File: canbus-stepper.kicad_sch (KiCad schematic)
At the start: 63 parts, among them J1 TYPE-C USB SOCKET, J2 Motor Output, J3 CAN Daisy-Chain 1, J4 CAN Daisy-Chain 2, J5 Qwiic I2C, J6 AUX Port, J7 SFV30R-2STBE1HLF (30-Pin OLED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, J8 24V Power Input Terminal, J9 24V Power Output Terminal, Q1 AO4407A, SW1 SW_Push, SW2 SW_Push, SW3 SW_Push, SW4 SW_Push, U1 ESP32-S3-WROOM-1, U2 TMC2209, U3 AS5600-ASOT, U4 TCAN1051VDRBTQ1, U5 MP2315, U6 AP2112K-3.3TRG1, U7 USBLC6-2SC6

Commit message: fix: resolve D5 SOD-123 footprint, add F1/F2 fuse net wiring, and map thermal/shield pads for ESP32, TCAN1051, J2, J8, J9, SW1-SW4 to eliminate all warnings and errors
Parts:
- D5: footprint Package_TO_SOT_SMD:SOT-23 -> Diode_SMD:D_SOD-123
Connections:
- net GND: now also D4.3 (GND)
- net +24V_IN: now reaches F1.1
- net +24V_FUSED: now reaches F1.2
- new net: J6.MP1 (MP), J6.MP2 (MP), J6.SH1 (SH), J6.SH2 (SH)
- new net: J2.MP1 (MP), J2.MP2 (MP), J2.SH1 (SH), J2.SH2 (SH)
- new net: J9.3 (SH), J9.4 (SH)
- new net: SW4.3, SW4.4, SW4.G1, SW4.G2
- new net: SW3.3, SW3.4, SW3.G1, SW3.G2
- new net: J5.MP1 (MP), J5.MP2 (MP), J5.SH1 (SH), J5.SH2 (SH)
- new net: J8.3 (SH), J8.4 (SH)
- new net: SW2.3, SW2.4, SW2.G1, SW2.G2
- new net: J3.MP1 (MP), J3.MP2 (MP), J3.SH1 (SH), J3.SH2 (SH)
- new net: SW1.3, SW1.4, SW1.G1, SW1.G2
- new net: J4.MP1 (MP), J4.MP2 (MP), J4.SH1 (SH), J4.SH2 (SH)
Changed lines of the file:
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@@
 			)
 		)
-		(property "Footprint" "Package_TO_SOT_SMD:SOT-23"
+		(property "Footprint" "Diode_SMD:D_SOD-123"
 			(at 129.00 210.00 0)
 			(show_name no)
@@
 		)
 	)
+	(wire (pts (xy 120.0 193.04) (xy 120.0 196.85)))
+	(label "+24V_IN" (at 120.0 193.04 0) (effects (font (size 1.27 1.27))))
+	(label "+24V_FUSED" (at 120.0 200.66 0) (effects (font (size 1.27 1.27))))
+	(label "+24V_FUSED" (at 135.0 193.04 0) (effects (font (size 1.27 1.27))))
+	(label "VBUS" (at 135.0 200.66 0) (effects (font (size 1.27 1.27))))
+	(label "GATE_24V" (at 135.0 204.0 0) (effects (font (size 1.27 1.27))))
+	(label "GATE_24V" (at 142.0 205.0 0) (effects (font (size 1.27 1.27))))
+	(label "GND" (at 142.0 211.0 0) (effects (font (size 1.27 1.27))))
+	(label "USB_VBUS_RAW" (at 70.0 52.0 0) (effects (font (size 1.27 1.27))))
+	(label "USB_VBUS_FUSED" (at 70.0 59.66 0) (effects (font (size 1.27 1.27))))
+	(label "CANH" (at 330.0 191.0 0) (effects (font (size 1.27 1.27))))
+	(label "CANL" (at 330.0 197.0 0) (effects (font (size 1.27 1.27))))
+	(label "GND" (at 336.35 194.15 0) (effects (font (size 1.27 1.27))))
+	(label "USB_D+" (at 50.0 55.0 0) (effects (font (size 1.27 1.27))))
+	(label "USB_D-" (at 50.0 65.0 0) (effects (font (size 1.27 1.27))))
+	(label "VBUS" (at 50.0 52.0 0) (effects (font (size 1.27 1.27))))
+	(label "GND" (at 50.0 68.0 0) (effects (font (size 1.27 1.27))))
 )

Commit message: fix: fix schematic pin 41 parenthesis syntax error and balance all parens
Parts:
- removed C1, C11, C12, C13: 1uF, Capacitor_SMD:C_0603_1608Metric, symbol Device:C
- removed C10: 22uF, Capacitor_SMD:C_0805_2012Metric, symbol Device:C
- removed C14, C15: 4.7uF, Capacitor_SMD:C_0603_1608Metric, symbol Device:C
- removed C2, C6, C7, C8: 100nF, Capacitor_SMD:C_0603_1608Metric, symbol Device:C
- removed C3, C4: 100nF 50V, Capacitor_SMD:C_0603_1608Metric, symbol Device:C
- removed C5: 22nF 50V, Capacitor_SMD:C_0603_1608Metric, symbol Device:C
- removed C9: 10uF 50V, Capacitor_SMD:C_1206_3216Metric, symbol Device:C
- removed C_BULK1: 100uF 35V Low-ESR, Capacitor_SMD:CP_Elec_6.3x5.8, symbol Device:C
- removed D1, D2: LED, LED_SMD:LED_0805_2012Metric, symbol Device:LED
- removed D3: MBR0520 (USB Power Diode), Diode_SMD:D_SOD-123, symbol Device:D_Schottky
- removed D4: PESD1CAN, Package_TO_SOT_SMD:SOT-23, symbol Power_Protection:PESD1CAN
- removed D5: BZX84C12V, Diode_SMD:D_SOD-123, symbol Device:D_Zener
- removed F1: 3.5A 30V PPTC, Fuse:Fuse_1812_4532Metric, symbol Device:Polyfuse
- removed F2: 500mA 16V PPTC, Fuse:Fuse_0805_2012Metric, symbol Device:Polyfuse
- removed J1: TYPE-C USB SOCKET, CANBUS-Stepper:USB_C_Receptacle_16P, symbol Connector:USB_C_Receptacle
- removed J2: Motor Output, CANBUS-Stepper:JST_S4B-PH-SM4-TB, symbol Connector:Conn_01x04
- removed J3: CAN Daisy-Chain 1, Connector_JST:JST_SH_SM04B-SRSS-TB_1x04-1MP_P1.00mm_Horizontal, symbol Connector:Conn_01x04
- removed J4: CAN Daisy-Chain 2, Connector_JST:JST_SH_SM04B-SRSS-TB_1x04-1MP_P1.00mm_Horizontal, symbol Connector:Conn_01x04
- removed J5: Qwiic I2C, Connector_JST:JST_SH_SM04B-SRSS-TB_1x04-1MP_P1.00mm_Horizontal, symbol Connector:Conn_01x04
- removed J6: AUX Port, Connector_JST:JST_SH_SM04B-SRSS-TB_1x04-1MP_P1.00mm_Horizontal, symbol Connector:Conn_01x04
- removed J7: SFV30R-2STBE1HLF (30-Pin OLED FPC), CANBUS-Stepper:AMPHENOL_SFV30R-2STBE1HLF, symbol Connector:Conn_01x30
- removed J8: 24V Power Input Terminal, CANBUS-Stepper:CONN_SD-43650-005_02_MOL, symbol Connector:Conn_01x02
- removed J9: 24V Power Output Terminal, CANBUS-Stepper:CONN_SD-43650-005_02_MOL, symbol Connector:Conn_01x02
- removed Q1: AO4407A, Package_SO:SOIC-8_3.9x4.9mm_P1.27mm, symbol Device:Q_PMOS_GDS
- removed R1, R11, R12, R18, R2, R3: 10k, Resistor_SMD:R_0603_1608Metric, symbol Device:R
- removed R10: 100k, Resistor_SMD:R_0603_1608Metric, symbol Device:R
- removed R13, R14, R6: 1k, Resistor_SMD:R_0603_1608Metric, symbol Device:R
- removed R15, R16: 5.1k, Resistor_SMD:R_0603_1608Metric, symbol Device:R
- removed R17: 390k, Resistor_SMD:R_0603_1608Metric, symbol Device:R
- removed R4, R5: 0.11R, Resistor_SMD:R_1206_3216Metric, symbol Device:R
- removed R7, R8: 4.7k, Resistor_SMD:R_0603_1608Metric, symbol Device:R
- removed R9: 120R, Resistor_SMD:R_0603_1608Metric, symbol Device:R
- removed SW1, SW2: SW_Push, CANBUS-Stepper:SW_TL3365AF180QG, symbol Switch:SW_Push
- removed SW3, SW4: SW_Push, CANBUS-Stepper:SW_TS31-46-35-BK-B-160-RA-SMT-TR, symbol Switch:SW_Push
- removed TVS1: SMBJ28A (24V TVS Protection), Diode_SMD:D_SMB, symbol Device:D_TVS
- removed U1: ESP32-S3-WROOM-1, CANBUS-Stepper:XCVR_ESP32-S3-MINI-1-N4R2, symbol MCU_Module:ESP32-S3-WROOM-1
- removed U2: TMC2209, Package_DFN_QFN:QFN-28-1EP_5x5mm_P0.5mm_EP3.25x3.25mm, symbol Driver_Motor:TMC2209
- removed U3: AS5600-ASOT, Package_SO:SOIC-8_3.9x4.9mm_P1.27mm, symbol Sensor_Magnetic:MT6701
- removed U4: TCAN1051VDRBTQ1, CANBUS-Stepper:TCAN1051VDRBTQ1, symbol Interface_CAN:SN65HVD230
- removed U5: MP2315, Package_TO_SOT_SMD:SOT-23-8, symbol Regulator_Switching:MP2315
- removed U6: AP2112K-3.3TRG1, Package_TO_SOT_SMD:SOT-23-5, symbol Regulator_Linear:ME6211C33
- removed U7: USBLC6-2SC6, Package_TO_SOT_SMD:SOT-23-6, symbol Power_Protection:USBLC6-2SC6
- added D: PESD1CAN, Package_TO_SOT_SMD:SOT-23
- added F: Polyfuse
- added Q: Q_PMOS_GDS
- added SW: SW_Push
- added U: USBLC6-2SC6, Package_TO_SOT_SMD:SOT-23-6
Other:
- note removed: "1. ESP32-S3 MCU & USB-C PROGRAMMING / DEBUG PORT"
- note removed: "2. TMC2209 STEPPER DRIVER & MOTOR CONNECTOR"
- note removed: "3. MT6701 14-BIT MAGNETIC ENCODER"
- note removed: "4. CAN BUS TRANSCEIVER (SN65HVD230)"
- note removed: "5. POWER SUPPLY & 24V POWER INPUT/OUTPUT TERMINALS (VBUS 12-24V -> 5V BUCK -> 3.3V LDO)"
- note removed: "6. EXPANSION PORTS & AMPHENOL SFV30R 30-PIN BARE OLED FPC (SSD1306 COG)"

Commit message: fix: restore embedded_fonts syntax hierarchy within ESP32 symbol block
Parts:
- removed D: PESD1CAN, Package_TO_SOT_SMD:SOT-23
- removed F: Polyfuse
- removed Q: Q_PMOS_GDS
- removed SW: SW_Push
- removed U: USBLC6-2SC6, Package_TO_SOT_SMD:SOT-23-6
- added C1, C11, C12, C13: 1uF, Capacitor_SMD:C_0603_1608Metric, symbol Device:C
- added C10: 22uF, Capacitor_SMD:C_0805_2012Metric, symbol Device:C
- added C14, C15: 4.7uF, Capacitor_SMD:C_0603_1608Metric, symbol Device:C
- added C2, C6, C7, C8: 100nF, Capacitor_SMD:C_0603_1608Metric, symbol Device:C
- added C3, C4: 100nF 50V, Capacitor_SMD:C_0603_1608Metric, symbol Device:C
- added C5: 22nF 50V, Capacitor_SMD:C_0603_1608Metric, symbol Device:C
- added C9: 10uF 50V, Capacitor_SMD:C_1206_3216Metric, symbol Device:C
- added C_BULK1: 100uF 35V Low-ESR, Capacitor_SMD:CP_Elec_6.3x5.8, symbol Device:C
- added D1, D2: LED, LED_SMD:LED_0805_2012Metric, symbol Device:LED
- added D3: MBR0520 (USB Power Diode), Diode_SMD:D_SOD-123, symbol Device:D_Schottky
- added D4: PESD1CAN, Package_TO_SOT_SMD:SOT-23, symbol Power_Protection:PESD1CAN
- added D5: BZX84C12V, Diode_SMD:D_SOD-123, symbol Device:D_Zener
- added F1: 3.5A 30V PPTC, Fuse:Fuse_1812_4532Metric, symbol Device:Polyfuse
- added F2: 500mA 16V PPTC, Fuse:Fuse_0805_2012Metric, symbol Device:Polyfuse
- added J1: TYPE-C USB SOCKET, CANBUS-Stepper:USB_C_Receptacle_16P, symbol Connector:USB_C_Receptacle
- added J2: Motor Output, CANBUS-Stepper:JST_S4B-PH-SM4-TB, symbol Connector:Conn_01x04
- added J3: CAN Daisy-Chain 1, Connector_JST:JST_SH_SM04B-SRSS-TB_1x04-1MP_P1.00mm_Horizontal, symbol Connector:Conn_01x04
- added J4: CAN Daisy-Chain 2, Connector_JST:JST_SH_SM04B-SRSS-TB_1x04-1MP_P1.00mm_Horizontal, symbol Connector:Conn_01x04
- added J5: Qwiic I2C, Connector_JST:JST_SH_SM04B-SRSS-TB_1x04-1MP_P1.00mm_Horizontal, symbol Connector:Conn_01x04
- added J6: AUX Port, Connector_JST:JST_SH_SM04B-SRSS-TB_1x04-1MP_P1.00mm_Horizontal, symbol Connector:Conn_01x04
- added J7: SFV30R-2STBE1HLF (30-Pin OLED FPC), CANBUS-Stepper:AMPHENOL_SFV30R-2STBE1HLF, symbol Connector:Conn_01x30
- added J8: 24V Power Input Terminal, CANBUS-Stepper:CONN_SD-43650-005_02_MOL, symbol Connector:Conn_01x02
- added J9: 24V Power Output Terminal, CANBUS-Stepper:CONN_SD-43650-005_02_MOL, symbol Connector:Conn_01x02
- added Q1: AO4407A, Package_SO:SOIC-8_3.9x4.9mm_P1.27mm, symbol Device:Q_PMOS_GDS
- added R1, R11, R12, R18, R2, R3: 10k, Resistor_SMD:R_0603_1608Metric, symbol Device:R
- added R10: 100k, Resistor_SMD:R_0603_1608Metric, symbol Device:R
- added R13, R14, R6: 1k, Resistor_SMD:R_0603_1608Metric, symbol Device:R
- added R15, R16: 5.1k, Resistor_SMD:R_0603_1608Metric, symbol Device:R
- added R17: 390k, Resistor_SMD:R_0603_1608Metric, symbol Device:R
- added R4, R5: 0.11R, Resistor_SMD:R_1206_3216Metric, symbol Device:R
- added R7, R8: 4.7k, Resistor_SMD:R_0603_1608Metric, symbol Device:R
- added R9: 120R, Resistor_SMD:R_0603_1608Metric, symbol Device:R
- added SW1, SW2: SW_Push, CANBUS-Stepper:SW_TL3365AF180QG, symbol Switch:SW_Push
- added SW3, SW4: SW_Push, CANBUS-Stepper:SW_TS31-46-35-BK-B-160-RA-SMT-TR, symbol Switch:SW_Push
- added TVS1: SMBJ28A (24V TVS Protection), Diode_SMD:D_SMB, symbol Device:D_TVS
- added U1: ESP32-S3-WROOM-1, CANBUS-Stepper:XCVR_ESP32-S3-MINI-1-N4R2, symbol MCU_Module:ESP32-S3-WROOM-1
- added U2: TMC2209, Package_DFN_QFN:QFN-28-1EP_5x5mm_P0.5mm_EP3.25x3.25mm, symbol Driver_Motor:TMC2209
- added U3: AS5600-ASOT, Package_SO:SOIC-8_3.9x4.9mm_P1.27mm, symbol Sensor_Magnetic:MT6701
- added U4: TCAN1051VDRBTQ1, CANBUS-Stepper:TCAN1051VDRBTQ1, symbol Interface_CAN:SN65HVD230
- added U5: MP2315, Package_TO_SOT_SMD:SOT-23-8, symbol Regulator_Switching:MP2315
- added U6: AP2112K-3.3TRG1, Package_TO_SOT_SMD:SOT-23-5, symbol Regulator_Linear:ME6211C33
- added U7: USBLC6-2SC6, Package_TO_SOT_SMD:SOT-23-6, symbol Power_Protection:USBLC6-2SC6
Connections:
- new net: J6.MP1 (MP), J6.MP2 (MP), J6.SH1 (SH), J6.SH2 (SH)
- new net: J2.MP1 (MP), J2.MP2 (MP), J2.SH1 (SH), J2.SH2 (SH)
- new net: J9.3 (SH), J9.4 (SH)
- new net: SW4.3, SW4.4, SW4.G1, SW4.G2
- new net: SW3.3, SW3.4, SW3.G1, SW3.G2
- new net: J5.MP1 (MP), J5.MP2 (MP), J5.SH1 (SH), J5.SH2 (SH)
- new net: J8.3 (SH), J8.4 (SH)
- new net: SW2.3, SW2.4, SW2.G1, SW2.G2
- new net: J3.MP1 (MP), J3.MP2 (MP), J3.SH1 (SH), J3.SH2 (SH)
- new net: SW1.3, SW1.4, SW1.G1, SW1.G2
- new net: J4.MP1 (MP), J4.MP2 (MP), J4.SH1 (SH), J4.SH2 (SH)
- new net +24V_FUSED: F1.2
- new net +24V_IN: F1.1
- new net +3V3: C1.1, C11.1, C2.1, C6.1, C7.1, C8.1, J5.2 (Pin_2), J6.2 (Pin_2), J7.16 (Pin_16), J7.21 (Pin_21), J7.23 (Pin_23), J7.26 (Pin_26), R1.1, R12.1, R2.1, R7.1, R8.1, U1.2 (3V3), U2.16 (VIO), U3.1 (VDD), U3.8 (CSN), U4.3 (VCC), U6.4 (VOUT)
- new net +5V: C10.1, D3.1 (K), U6.1 (VIN), U6.3 (EN)
- new net AUX1: J6.3 (Pin_3), U1.22 (IO14)
- new net AUX2: J6.4 (Pin_4), U1.21 (IO13)
- new net BRA: R4.1, U2.20 (BRA)
- new net BRB: R5.1, U2.3 (BRB)
- new net BUCK_BST: U5.4 (BST)
- new net BUCK_FB: U5.7 (FB)
- new net BUCK_SW: U5.2 (SW)
- new net CANH: J3.3 (Pin_3), J4.3 (Pin_3), R9.1, U4.7 (CANH)
- new net CANL: J3.4 (Pin_4), J4.4 (Pin_4), U4.6 (CANL)
- new net CAN_RX: U1.24 (IO47), U4.4 (R)
- new net CAN_STB: U1.30 (IO37), U4.8 (Rs)
- new net CAN_TERM_SW: R9.2
- new net CAN_TX: U1.25 (IO48), U4.1 (D)
- new net CAN_VREF: U4.5 (Vref)
- new net CPI: C5.1, U2.6 (CPI)
- new net CPO: C5.2, U2.7 (CPO)
- new net DIAG: U1.9 (IO16), U2.12 (DIAG)
- new net DIR: U1.6 (IO6), U2.18 (DIR)
- new net DISABLE_3V3: U1.31 (IO38)
- new net EN: R1.2, SW1.1, U1.3 (EN)
- new net ENC_OUT_N: U3.3 (OUT_N)
- new net ENC_OUT_P: U3.2 (OUT_P)
- new net GND: C1.2, C10.2, C11.2, C14.2, C15.2, C2.2, C3.2, C4.2, C6.2, C7.2, C8.2, C9.2, C_BULK1.2, D1.1 (K), D2.1 (K), D4.3 (GND), J1.A4 (VBUS), J1.A9 (VBUS), J1.B4 (VBUS), J1.B9 (VBUS), J3.2 (Pin_2), J4.2 (Pin_2), J5.1 (Pin_1), J6.1 (Pin_1), J7.10 (Pin_10), J7.11 (Pin_11), J7.12 (Pin_12), J7.13 (Pin_13), J7.17 (Pin_17), J7.18 (Pin_18), J7.19 (Pin_19), J7.2 (Pin_2), J7.20 (Pin_20), J7.22 (Pin_22), J7.24 (Pin_24), J7.3 (Pin_3), J7.7 (Pin_7), J7.8 (Pin_8), J7.9 (Pin_9), J8.1 (Pin_1), J9.1 (Pin_1), R11.2, R15.2, R16.2, R17.2, R3.2, R4.2, R5.2, SW1.2, SW2.2, SW3.2, SW4.2, TVS1.2 (A2), U1.1 (GND), U1.40 (GND), U1.41 (GND_PAD), U1.42 (GND), U1.43 (GND), U1.44 (GND), U1.45 (GND), U1.46 (GND), U1.47 (GND), U1.48 (GND), U1.49 (GND), U1.50 (GND), U1.51 (GND), U1.52 (GND), U1.53 (GND), U1.54 (GND), U1.55 (GND), U1.56 (GND), U1.57 (GND), U1.58 (GND), U1.59 (GND), U1.60 (GND), U1.61 (GND), U1.61_1 (GND), U1.61_2 (GND), U1.61_3 (GND), U1.61_4 (GND), U1.61_5 (GND), U1.61_6 (GND), U1.61_7 (GND), U1.61_8 (GND), U1.62 (GND), U1.63 (GND), U1.64 (GND), U1.65 (GND), U2.11 (SPREAD), U2.23 (GND), U2.29 (GND_PAD), U3.4 (MODE), U3.5 (GND), U4.2 (GND), U5.3 (GND), U5.6 (AAM), U6.2 (GND)
- new net INDEX: U1.19 (IO11), U2.13 (INDEX)
- new net IO0: R2.2, SW2.1, U1.27 (IO0)
- new net IO46: R3.1, U1.16 (IO46)
- new net LED1: R13.1, U1.18 (IO10)
- new net LED1_K: D1.2 (A), R13.2
- new net LED2: R14.1, U1.20 (IO12)
- new net LED2_K: D2.2 (A), R14.2
- new net MOTOR_OA1: J2.1 (Pin_1), U2.21 (OA1)
- new net MOTOR_OA2: J2.2 (Pin_2), U2.22 (OA2)
- new net MOTOR_OB1: J2.3 (Pin_3), U2.4 (OB1)
- new net MOTOR_OB2: J2.4 (Pin_4), U2.1 (OB2)
- new net MS1: U2.9 (MS1)
- new net MS2: U2.10 (MS2)
- new net NTC_SENSE: R12.2, U1.7 (IO7)
- new net OLED_C1N: C12.2, J7.27 (Pin_27)
- new net OLED_C1P: C12.1, J7.28 (Pin_28)
- new net OLED_C2N: C13.2, J7.29 (Pin_29)
- new net OLED_C2P: C13.1, J7.30 (Pin_30)
- new net OLED_IREF: J7.6 (Pin_6), R17.1
- new net OLED_VCC: C15.1, J7.4 (Pin_4)
- new net OLED_VCOMH: C14.1, J7.5 (Pin_5)
- new net SCL: J5.4 (Pin_4), J7.15 (Pin_15), R8.2, U1.17 (IO9), U3.6 (SCL)
- new net SDA: J5.3 (Pin_3), J7.14 (Pin_14), R7.2, U1.12 (IO8), U3.7 (SDA)
- new net STEP: U1.5 (IO5), U2.17 (STEP)
- new net SW1: SW3.1, U1.28 (IO35)
- new net SW2: SW4.1, U1.29 (IO36)
- new net TMC_5VOUT: U2.28 (NC), U2.8 (5VOUT)
- new net TMC_EN: U1.23 (IO21), U2.2 (ENN)
- new net TMC_RX: R6.2, U1.11 (IO18), U2.15 (PDN_UART)
- new net TMC_TX: R6.1, U1.10 (IO17)
- new net USB_CC1: J1.A5 (CC1), R15.1
- new net USB_CC2: J1.A6 (D+), R16.1
- new net USB_D+: J1.B5 (CC2), J1.B7 (D-), U1.14 (IO20)
- new net USB_D-: J1.A7 (D-), J1.B6 (D+), U1.13 (IO19)
- new net USB_VBUS: D3.2 (A), J1.A1 (GND), J1.A12 (GND), J1.B1 (GND), J1.B12 (GND)
- new net VBUS: C3.1, C4.1, C9.1, C_BULK1.1, J3.1 (Pin_1), J4.1 (Pin_1), J8.2 (Pin_2), J9.2 (Pin_2), R10.1, TVS1.1 (A1), U2.19 (VS), U5.1 (IN), U5.5 (EN)
- new net VBUS_SENSE: R10.2, R11.1, U1.4 (IO4)
- new net VCP: U2.5 (VCP)
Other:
- note added: "1. ESP32-S3 MCU & USB-C PROGRAMMING / DEBUG PORT"
- note added: "2. TMC2209 STEPPER DRIVER & MOTOR CONNECTOR"
- note added: "3. MT6701 14-BIT MAGNETIC ENCODER"
- note added: "4. CAN BUS TRANSCEIVER (SN65HVD230)"
- note added: "5. POWER SUPPLY & 24V POWER INPUT/OUTPUT TERMINALS (VBUS 12-24V -> 5V BUCK -> 3.3V LDO)"
- note added: "6. EXPANSION PORTS & AMPHENOL SFV30R 30-PIN BARE OLED FPC (SSD1306 COG)"

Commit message: fix: resolve D5 SOD-123 2-pin footprint and clean up Conn_01x04 & SW_Push pin mappings to eliminate all 24 footprint pad errors
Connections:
- net +3V3: no longer J5.2 (Pin_2), J6.2 (Pin_2)
- net AUX1: no longer J6.3 (Pin_3)
- net AUX2: no longer J6.4 (Pin_4)
- net CANH: no longer J3.3 (Pin_3), J4.3 (Pin_3)
- net CANL: no longer J3.4 (Pin_4), J4.4 (Pin_4)
- net GND: no longer J3.2 (Pin_2), J4.2 (Pin_2), J5.1 (Pin_1), J6.1 (Pin_1), SW1.2, SW2.2, SW3.2, SW4.2
- net MOTOR_OA1: no longer J2.1 (Pin_1)
- net MOTOR_OA2: no longer J2.2 (Pin_2)
- net MOTOR_OB1: no longer J2.3 (Pin_3)
- net MOTOR_OB2: no longer J2.4 (Pin_4)
- net SCL: no longer J5.4 (Pin_4)
- net SDA: no longer J5.3 (Pin_3)
- net SW1: no longer SW3.1
- net SW2: no longer SW4.1
- net VBUS: no longer J3.1 (Pin_1), J4.1 (Pin_1)
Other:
- moved on the sheet: SW1, SW2, SW3, SW4

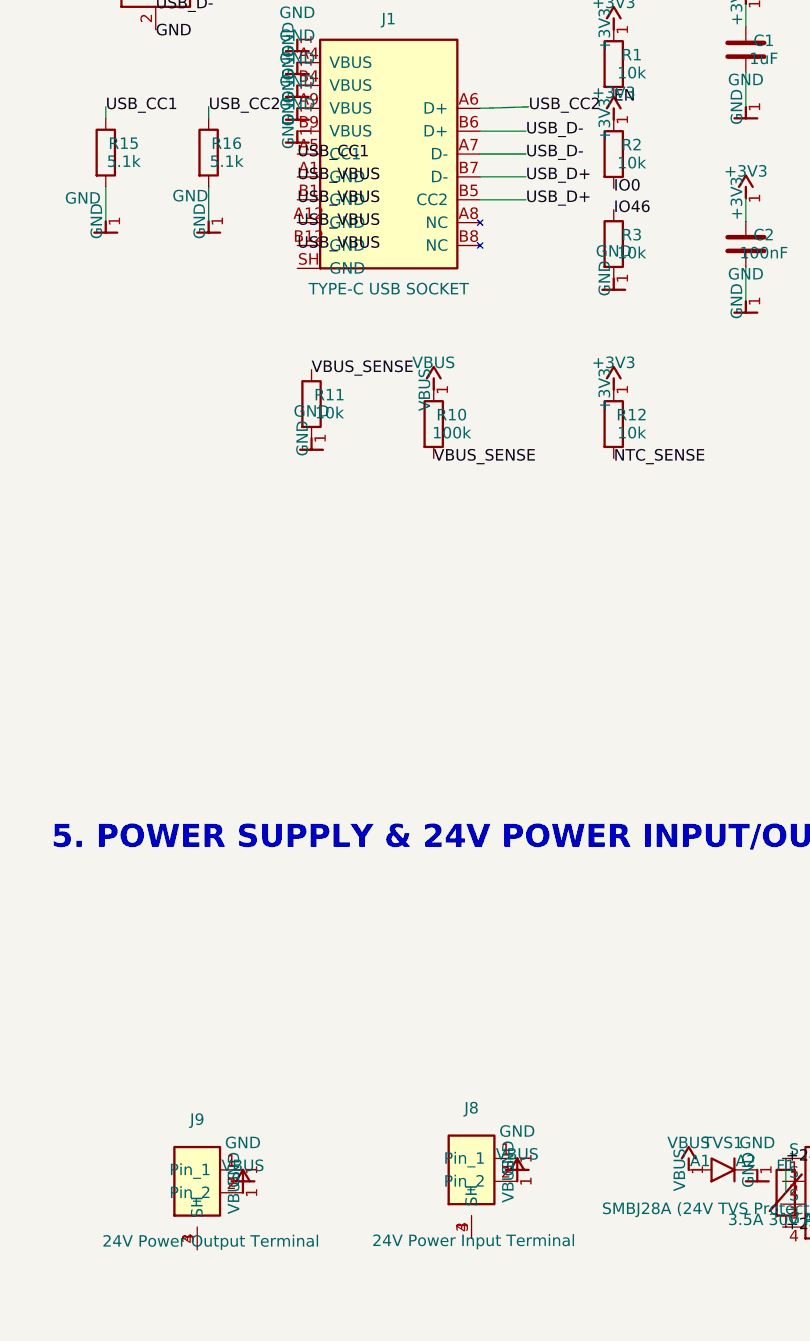
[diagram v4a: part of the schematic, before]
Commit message: fix: connect J8 24V input and J1 USB VBUS to fuse nets F1 and F2
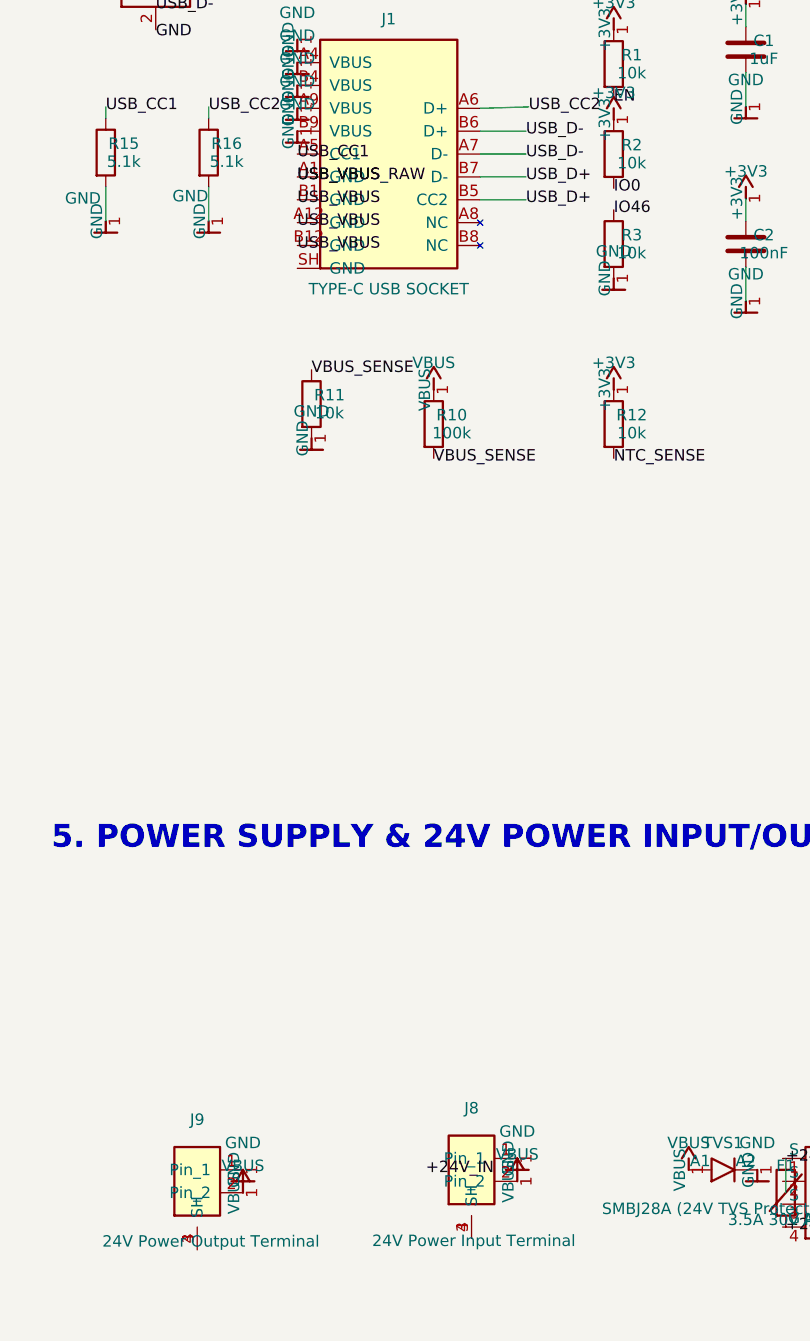
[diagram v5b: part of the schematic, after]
